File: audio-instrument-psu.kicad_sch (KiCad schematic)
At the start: 48 parts, among them J1 Molex_SL_01x04_Male, J2 Molex_SL_01x04_Male, J3 Molex_SL_01x04_Male, J4 Molex_SL_01x04_Male, J5 Molex_SL_01x04_Male, J99 Mini-DIN-4, U1 LM317_TO-220, U2 LM337_TO220

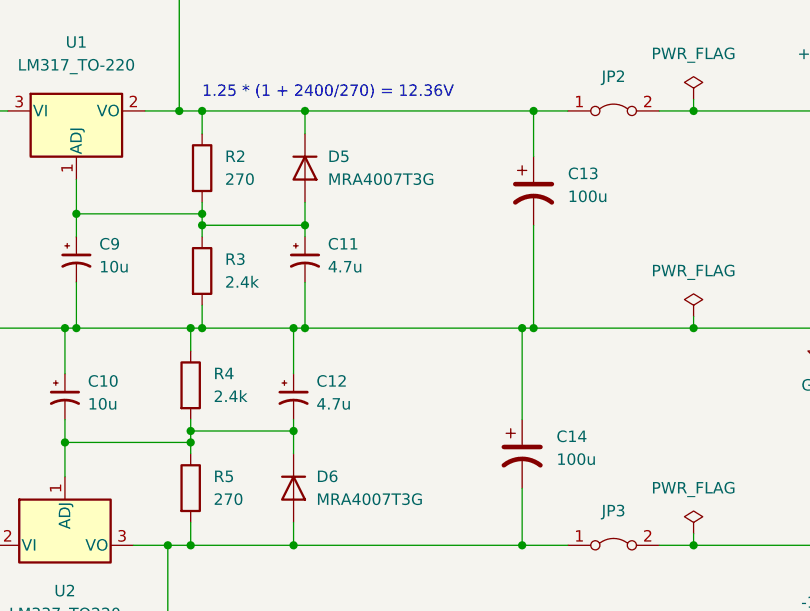
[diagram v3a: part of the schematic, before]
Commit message: remove redundant ADJ caps
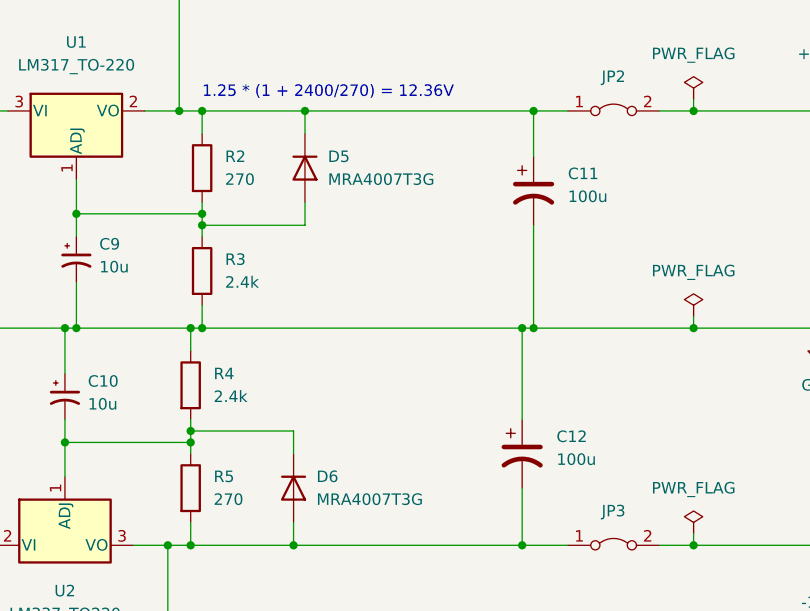
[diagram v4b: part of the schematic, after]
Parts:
- removed C11, C12: 4.7u, Capacitor_THT:CP_Radial_D5.0mm_P2.00mm, symbol Device:C_Polarized_Small_US
- renumbered C13 to C11, C14 to C12
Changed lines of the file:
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@@
   (junction (at 337.82 114.3) (diameter 0) (color 0 0 0 0)
   )
-  (junction (at 246.38 147.32) (diameter 0) (color 0 0 0 0)
-  )
   (junction (at 182.88 123.19) (diameter 0) (color 0 0 0 0)
   )
@@
   (junction (at 337.82 167.64) (diameter 0) (color 0 0 0 0)
   )
-  (junction (at 247.65 135.89) (diameter 0) (color 0 0 0 0)
-  )
   (junction (at 236.22 147.32) (diameter 0) (color 0 0 0 0)
   )
   (junction (at 271.78 147.32) (diameter 0) (color 0 0 0 0)
   )
-  (junction (at 246.38 158.75) (diameter 0) (color 0 0 0 0)
-  )
   (junction (at 236.22 134.62) (diameter 0) (color 0 0 0 0)
   )
@@
   (junction (at 273.05 123.19) (diameter 0) (color 0 0 0 0)
   )
-  (junction (at 247.65 147.32) (diameter 0) (color 0 0 0 0)
-  )
   (junction (at 236.22 123.19) (diameter 0) (color 0 0 0 0)
   )
@@
     (stroke (width 0) (type default) (color 0 0 0 0))
   )
-  (wire (pts (xy 247.65 142.24) (xy 247.65 147.32))
-    (stroke (width 0) (type default) (color 0 0 0 0))
-  )
   (wire (pts (xy 224.79 190.5) (xy 232.41 190.5))
     (stroke (width 0) (type default) (color 0 0 0 0))
@@
     (stroke (width 0) (type default) (color 0 0 0 0))
   )
-  (wire (pts (xy 246.38 147.32) (xy 246.38 152.4))
-    (stroke (width 0) (type default) (color 0 0 0 0))
-  )
   (wire (pts (xy 247.65 133.35) (xy 247.65 135.89))
     (stroke (width 0) (type default) (color 0 0 0 0))
@@
     (stroke (width 0) (type default) (color 0 0 0 0))
   )
-  (wire (pts (xy 247.65 147.32) (xy 271.78 147.32))
+  (wire (pts (xy 236.22 147.32) (xy 271.78 147.32))
     (stroke (width 0) (type default) (color 0 0 0 0))
   )
@@
     (stroke (width 0) (type default) (color 0 0 0 0))
   )
-  (wire (pts (xy 236.22 147.32) (xy 246.38 147.32))
-    (stroke (width 0) (type default) (color 0 0 0 0))
-  )
   (wire (pts (xy 326.39 195.58) (xy 326.39 199.39))
     (stroke (width 0) (type default) (color 0 0 0 0))
@@
     (stroke (width 0) (type default) (color 0 0 0 0))
   )
-  (wire (pts (xy 247.65 135.89) (xy 247.65 137.16))
-    (stroke (width 0) (type default) (color 0 0 0 0))
-  )
   (wire (pts (xy 97.79 147.32) (xy 167.64 147.32))
     (stroke (width 0) (type default) (color 0 0 0 0))
@@
     (stroke (width 0) (type default) (color 0 0 0 0))
   )
-  (wire (pts (xy 246.38 157.48) (xy 246.38 158.75))
-    (stroke (width 0) (type default) (color 0 0 0 0))
-  )
   (wire (pts (xy 335.28 201.93) (xy 337.82 201.93))
     (stroke (width 0) (type default) (color 0 0 0 0))
@@
   )
   (wire (pts (xy 168.91 123.19) (xy 182.88 123.19))
-    (stroke (width 0) (type default) (color 0 0 0 0))
-  )
-  (wire (pts (xy 247.65 147.32) (xy 246.38 147.32))
     (stroke (width 0) (type default) (color 0 0 0 0))
   )
@@
     (pin "2")
   )
-  (symbol (lib_id "Device:C_Polarized_Small_US") (at 247.65 139.7 0) (unit 1)
-    (in_bom yes) (on_board yes) (fields_autoplaced)
-    (property "Reference" "C11" (id 0) (at 250.19 137.9981 0)
-      (effects (font (size 1.27 1.27)) (justify left))
-    )
-    (property "Value" "4.7u" (id 1) (at 250.19 140.5381 0)
-      (effects (font (size 1.27 1.27)) (justify left))
-    )
-    (property "Footprint" "Capacitor_THT:CP_Radial_D5.0mm_P2.00mm" (id 2) (at 247.65 139.7 0)
-      (effects (font (size 1.27 1.27)) hide)
-    )
-    (property "Datasheet" "https://www.nichicon.co.jp/english/products/pdfs/e-uvr.pdf" (id 3) (at 247.65 139.7 0)
-      (effects (font (size 1.27 1.27)) hide)
-    )
-    (property "Dielectric" "Electrolytic" (id 4) (at 247.65 139.7 0)
-      (effects (font (size 1.27 1.27)) hide)
-    )
-    (property "Distributor" "Digikey" (id 5) (at 247.65 139.7 0)
-      (effects (font (size 1.27 1.27)) hide)
-    )
-    (property "Distributor PN" "493-1076-ND" (id 6) (at 247.65 139.7 0)
-      (effects (font (size 1.27 1.27)) hide)
-    )
-    (property "Manufacturer" "Nichicon" (id 7) (at 247.65 139.7 0)
-      (effects (font (size 1.27 1.27)) hide)
-    )
-    (property "Manufacturer PN" "UVR1V4R7MDD" (id 8) (at 247.65 139.7 0)
-      (effects (font (size 1.27 1.27)) hide)
-    )
-    (property "Voltage Rating" "35V" (id 9) (at 247.65 139.7 0)
-      (effects (font (size 1.27 1.27)) hide)
-    )
-    (pin "1")
-    (pin "2")
-  )
   (symbol (lib_id "Device:C_Polarized_Small_US") (at 222.25 139.7 0) (unit 1)
     (in_bom yes) (on_board yes) (fields_autoplaced)
@@
   (symbol (lib_id "Device:C_Polarized_US") (at 273.05 132.08 0) (unit 1)
     (in_bom yes) (on_board yes) (fields_autoplaced)
-    (property "Reference" "C13" (id 0) (at 276.86 130.1749 0)
+    (property "Reference" "C11" (id 0) (at 276.86 130.1749 0)
       (effects (font (size 1.27 1.27)) (justify left))
     )
@@
     )
     (pin "1")
-  )
-  (symbol (lib_id "Device:C_Polarized_Small_US") (at 246.38 154.94 0) (unit 1)
-    (in_bom yes) (on_board yes) (fields_autoplaced)
-    (property "Reference" "C12" (id 0) (at 248.92 153.2381 0)
-      (effects (font (size 1.27 1.27)) (justify left))
-    )
-    (property "Value" "4.7u" (id 1) (at 248.92 155.7781 0)
-      (effects (font (size 1.27 1.27)) (justify left))
-    )
-    (property "Footprint" "Capacitor_THT:CP_Radial_D5.0mm_P2.00mm" (id 2) (at 246.38 154.94 0)
-      (effects (font (size 1.27 1.27)) hide)
-    )
-    (property "Datasheet" "https://www.nichicon.co.jp/english/products/pdfs/e-uvr.pdf" (id 3) (at 246.38 154.94 0)
-      (effects (font (size 1.27 1.27)) hide)
-    )
-    (property "Dielectric" "Electrolytic" (id 4) (at 246.38 154.94 0)
-      (effects (font (size 1.27 1.27)) hide)
-    )
-    (property "Distributor" "Digikey" (id 5) (at 246.38 154.94 0)
-      (effects (font (size 1.27 1.27)) hide)
-    )
-    (property "Distributor PN" "493-1076-ND" (id 6) (at 246.38 154.94 0)
-      (effects (font (size 1.27 1.27)) hide)
-    )
-    (property "Manufacturer" "Nichicon" (id 7) (at 246.38 154.94 0)
-      (effects (font (size 1.27 1.27)) hide)
-    )
-    (property "Manufacturer PN" "UVR1V4R7MDD" (id 8) (at 246.38 154.94 0)
-      (effects (font (size 1.27 1.27)) hide)
-    )
-    (property "Voltage Rating" "35V" (id 9) (at 246.38 154.94 0)
-      (effects (font (size 1.27 1.27)) hide)
-    )
-    (pin "1")
-    (pin "2")
   )
   (symbol (lib_id "Regulator_Linear:LM317_TO-220") (at 222.25 123.19 0) (unit 1)
@@
   (symbol (lib_id "Device:C_Polarized_US") (at 271.78 161.29 0) (unit 1)
     (in_bom yes) (on_board yes) (fields_autoplaced)
-    (property "Reference" "C14" (id 0) (at 275.59 159.3849 0)
+    (property "Reference" "C12" (id 0) (at 275.59 159.3849 0)
       (effects (font (size 1.27 1.27)) (justify left))
     )
@@
       (reference "C10") (unit 1) (value "10u") (footprint "Capacitor_THT:CP_Radial_D5.0mm_P2.50mm")
     )
-    (path "/3a9b89fe-8589-4283-ad7d-36b3927932a2"
-      (reference "C11") (unit 1) (value "4.7u") (footprint "Capacitor_THT:CP_Radial_D5.0mm_P2.00mm")
-    )
-    (path "/97571ff8-0bc5-46a6-a426-19e59541490c"
-      (reference "C12") (unit 1) (value "4.7u") (footprint "Capacitor_THT:CP_Radial_D5.0mm_P2.00mm")
-    )
     (path "/8598cd5d-3dc1-404f-95b6-4d126d9a2e14"
-      (reference "C13") (unit 1) (value "100u") (footprint "Capacitor_THT:CP_Radial_D6.3mm_P2.50mm")
+      (reference "C11") (unit 1) (value "100u") (footprint "Capacitor_THT:CP_Radial_D6.3mm_P2.50mm")
     )
     (path "/ad769147-c5f9-4730-afda-189bfe47934c"
-      (reference "C14") (unit 1) (value "100u") (footprint "Capacitor_THT:CP_Radial_D6.3mm_P2.50mm")
+      (reference "C12") (unit 1) (value "100u") (footprint "Capacitor_THT:CP_Radial_D6.3mm_P2.50mm")
     )
     (path "/1986e4ae-9305-4ed5-b563-6cf9297e079c"
